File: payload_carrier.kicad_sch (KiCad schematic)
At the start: 44 parts, among them J1 Conn_01x02, J2 USB_C_Receptacle_USB2.0_16P, J3 Conn_01x08, J4 Conn_01x08, J5 Conn_01x05, J6 Micro_SD_Card, SW1 SW_MEC_5G, U1 TPS73733DCQR, U2 TPS562242DRLR, U3 STM32G0B1CBTx, Y1 Crystal

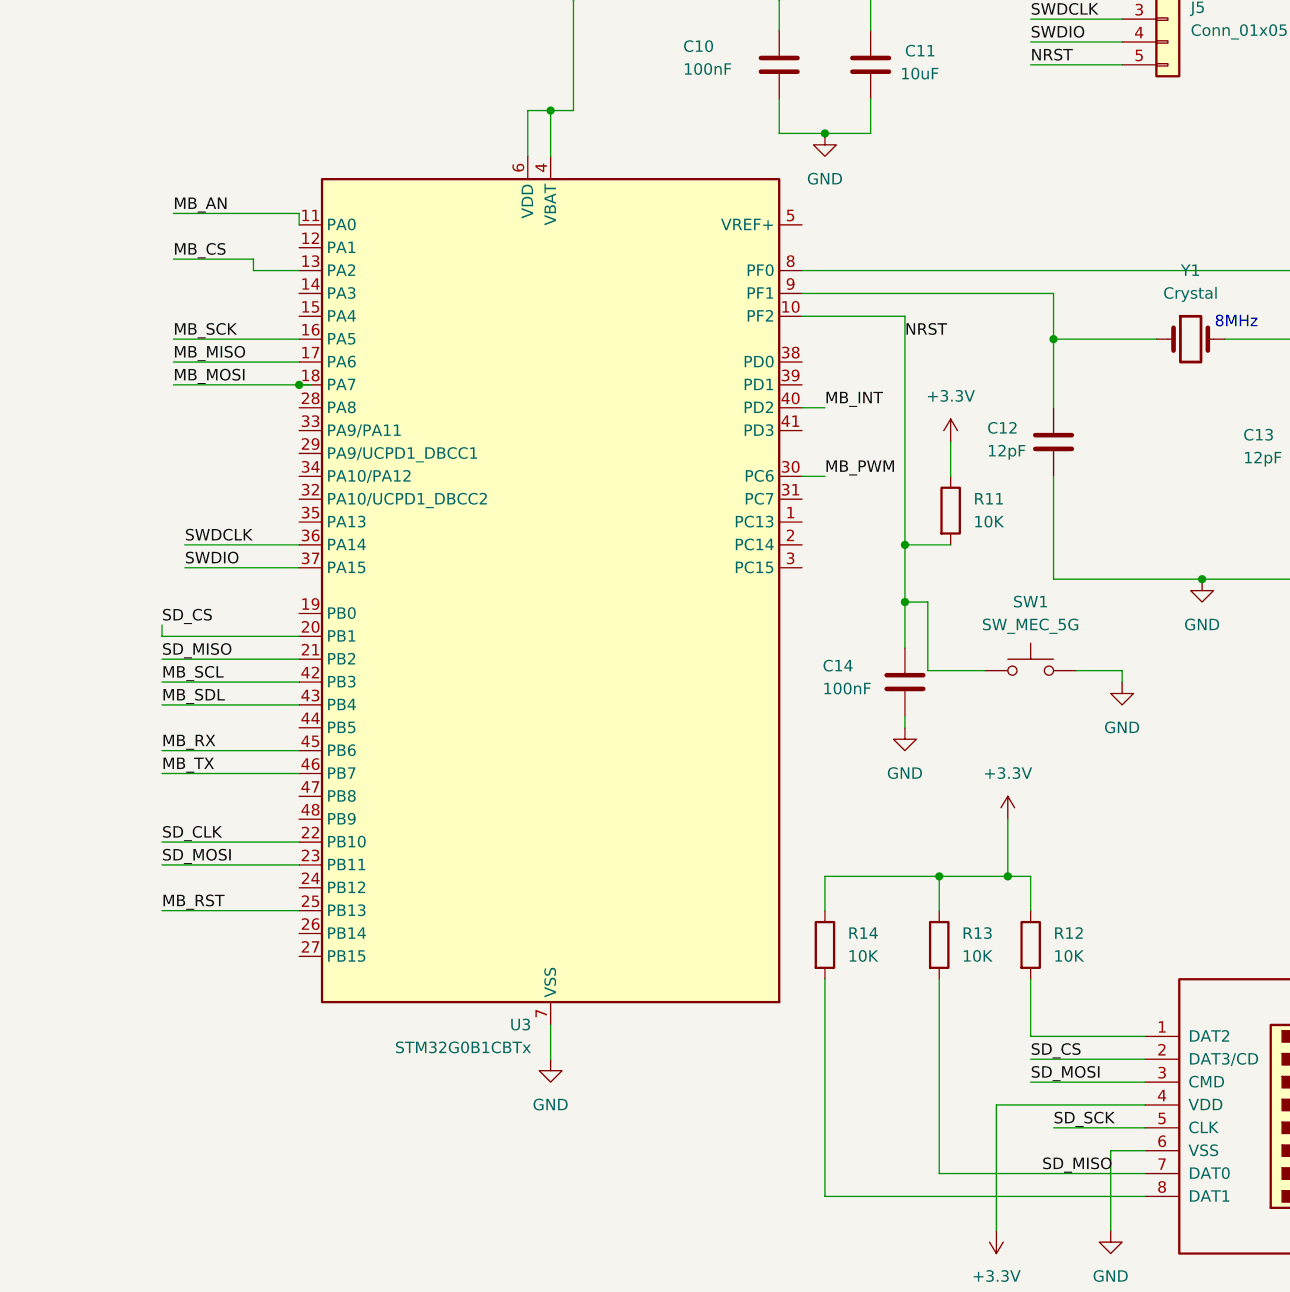
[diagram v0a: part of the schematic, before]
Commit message: Fix net bugs and assign footprints for layout session
- SD_SCK label -> SD_CLK: SD card CLK now reaches PB10
- MB_SDL label -> MB_SDA: PB4 now reaches mikroBUS SDA
- SWDIO moved from PA15 to PA13
- U1 footprint uses project lib nickname "My footprints"
- VREF+ tied to +3.3V with new C15 100nF decoupling
- Footprints on all parts except R11, C10, U2 (left for the
  footprint demo; stock 0603 R/C and SOT-563)
- Y1 on 2-pad 5032 crystal, SW1 on SW_MEC_5GSH9 (pads match symbol),
  D1/D2 on SMA (value should read B340A)

Co-Authored-By: Claude Opus 5.5 <noreply@anthropic.com>
Claude-Session: https://claude.ai/code/session_01BZgeQ4ki9vnPRRu7w6dazn
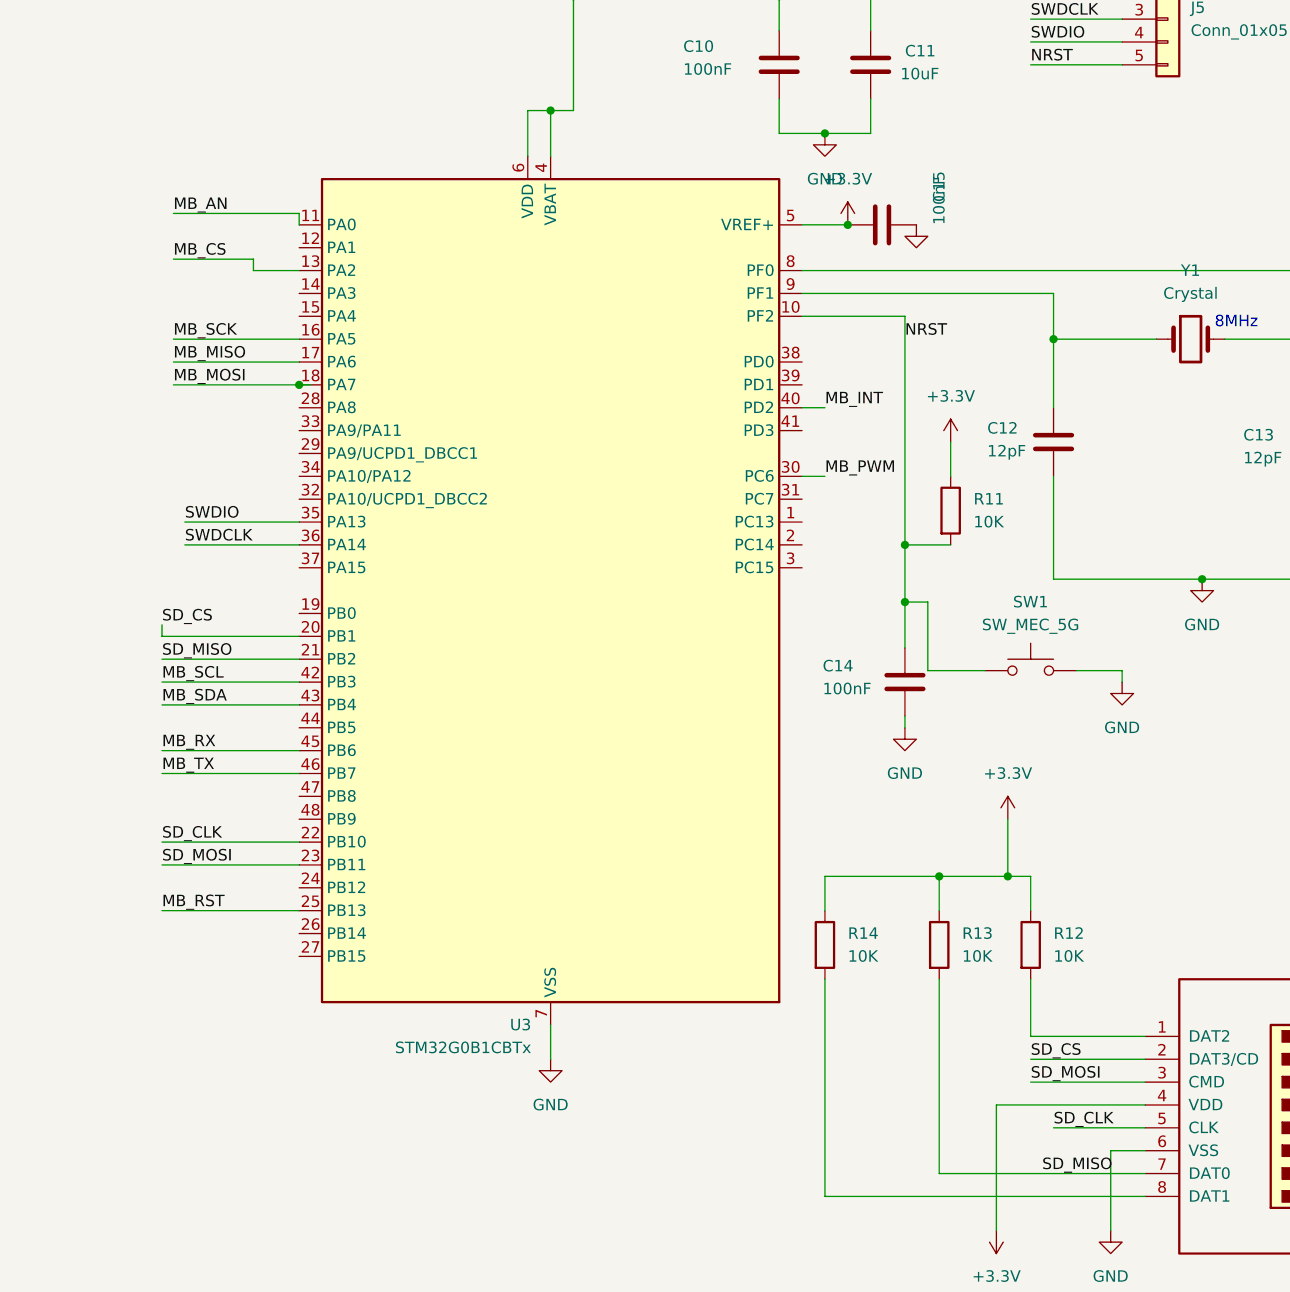
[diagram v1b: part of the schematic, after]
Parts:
- added C15: 100nF, Capacitor_SMD:C_0603_1608Metric, symbol KiCad:C
- C1, C12, C13, C14, C2, C3, C6, C7, C9: footprint (none) -> Capacitor_SMD:C_0603_1608Metric
- C11, C4, C5, C8: footprint (none) -> Capacitor_SMD:C_0805_2012Metric
- D1, D2: footprint (none) -> Diode_SMD:D_SMA
- D3, D4: footprint (none) -> LED_SMD:LED_0603_1608Metric
- J1: footprint (none) -> Connector_JST:JST_PH_B2B-PH-K_1x02_P2.00mm_Vertical
- J2: footprint (none) -> Connector_USB:USB_C_Receptacle_HRO_TYPE-C-31-M-12
- J3, J4: footprint (none) -> Connector_PinSocket_2.54mm:PinSocket_1x08_P2.54mm_Vertical
- J5: footprint (none) -> Connector_PinHeader_2.54mm:PinHeader_1x05_P2.54mm_Vertical
- J6: footprint (none) -> Connector_Card:microSD_HC_Wuerth_693072010801
- L1: footprint (none) -> Inductor_SMD:L_Bourns-SRN4018
- R1, R10, R12, R13, R14, R2, R3, R4, R5, R6, R7, R8, R9: footprint (none) -> Resistor_SMD:R_0603_1608Metric
- SW1: footprint (none) -> Button_Switch_SMD:SW_MEC_5GSH9
- U1: footprint TPS73733DCQR:IC_TPS73733DCQR -> My footprints:IC_TPS73733DCQR
- U2: footprint Package_TO_SOT_SMD:SOT-563 -> (none)
- Y1: footprint (none) -> Crystal:Crystal_SMD_5032-2Pin_5.0x3.2mm
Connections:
- net MB_SDL is gone; now on net MB_SDA: U3.43 (PB4)
- net SD_SCK is gone; now on net SD_CLK: J6.5 (CLK)
- net +3.3V: now also U3.5 (VREF+), C15.1
- net GND: now also C15.2
- net SWDIO: now also U3.35 (PA13); no longer U3.37 (PA15)

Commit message: Wire USB data to STM32, add buck feedforward cap, pick L1
- J2 D+ (A6/B6) -> PA12 (USB_DP), D- (A7/B7) -> PA11 (USB_DM);
  removed the four no-connect flags
- C16 33pF across R3 (TI TPS562242 Table 8-2, 5 V row)
- L1: Wurth WE-MAPI 4020 74438356033 (3.3uH, Isat 3.55A @10%),
  footprint Inductor_SMD:L_Wuerth_MAPI-4020

Co-Authored-By: Claude Opus 5.5 <noreply@anthropic.com>
Claude-Session: https://claude.ai/code/session_01BZgeQ4ki9vnPRRu7w6dazn
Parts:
- added C16: 33pF, Capacitor_SMD:C_0603_1608Metric, symbol KiCad:C
- L1: footprint Inductor_SMD:L_Bourns-SRN4018 -> Inductor_SMD:L_Wuerth_MAPI-4020
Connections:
- net at C8.1, C9.1, D1.2 (A)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: now also C16.1
- net USB_DM: now reaches U3.33 (PA9/PA11)
- net USB_DM: now also J2.A7 (D-), J2.B7 (D-)
- net USB_DP: now reaches U3.34 (PA10/PA12)
- net USB_DP: now also J2.A6 (D+), J2.B6 (D+)
- net at R3.2, R4.1, U2.6 (VFB): now also C16.2
- no-connect marks 6 -> 2
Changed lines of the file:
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@@
 	)
 	(no_connect
-		(at 199.39 76.2)
-	)
-	(no_connect
 		(at 209.55 76.2)
 	)
 	(no_connect
-		(at 194.31 76.2)
-	)
-	(no_connect
-		(at 196.85 76.2)
-	)
-	(no_connect
-		(at 191.77 76.2)
-	)
-	(no_connect
 		(at 207.01 76.2)
 	)
@@
 			)
 		)
-		(property "Footprint" "Inductor_SMD:L_Bourns-SRN4018"
+		(property "Footprint" "Inductor_SMD:L_Wuerth_MAPI-4020"
 			(at 166.37 33.02 0)
 			(hide yes)
@@
 			)
 		)
-		(property "Datasheet" ""
+		(property "Datasheet" "https://www.we-online.com/components/products/datasheet/74438356033.pdf"
 			(at 166.37 33.02 0)
 			(hide yes)
@@
 			)
 		)
-		(property "Description" "Inductor"
+		(property "Description" "Inductor, Wurth WE-MAPI 4020 74438356033, 3.3uH, Isat 3.55A"
 			(at 166.37 33.02 0)
 			(hide yes)
@@
 		)
 	)
+	(wire
+		(pts
+			(xy 191.77 76.2) (xy 191.77 73.66)
+		)
+		(stroke
+			(width 0)
+			(type default)
+		)
+	)
+	(wire
+		(pts
+			(xy 194.31 76.2) (xy 194.31 73.66)
+		)
+		(stroke
+			(width 0)
+			(type default)
+		)
+	)
+	(wire
+		(pts
+			(xy 191.77 73.66) (xy 194.31 73.66)
+		)
+		(stroke
+			(width 0)
+			(type default)
+		)
+	)
+	(label "USB_DM"
+		(at 191.77 73.66 0)
+		(effects
+			(font
+				(size 1.27 1.27)
+			)
+			(justify left bottom)
+		)
+	)
+	(wire
+		(pts
+			(xy 196.85 76.2) (xy 196.85 74.93)
+		)
+		(stroke
+			(width 0)
+			(type default)
+		)
+	)
+	(wire
+		(pts
+			(xy 199.39 76.2) (xy 199.39 74.93)
+		)
+		(stroke
+			(width 0)
+			(type default)
+		)
+	)
+	(wire
+		(pts
+			(xy 196.85 74.93) (xy 199.39 74.93)
+		)
+		(stroke
+			(width 0)
+			(type default)
+		)
+	)
+	(label "USB_DP"
+		(at 199.39 74.93 0)
+		(effects
+			(font
+				(size 1.27 1.27)
+			)
+			(justify left bottom)
+		)
+	)
+	(wire
+		(pts
+			(xy 71.12 182.88) (xy 83.82 182.88)
+		)
+		(stroke
+			(width 0)
+			(type default)
+		)
+	)
+	(label "USB_DM"
+		(at 71.12 182.88 0)
+		(effects
+			(font
+				(size 1.27 1.27)
+			)
+			(justify left bottom)
+		)
+	)
+	(wire
+		(pts
+			(xy 71.12 187.96) (xy 83.82 187.96)
+		)
+		(stroke
+			(width 0)
+			(type default)
+		)
+	)
+	(label "USB_DP"
+		(at 71.12 187.96 0)
+		(effects
+			(font
+				(size 1.27 1.27)
+			)
+			(justify left bottom)
+		)
+	)
+	(symbol
+		(lib_id "KiCad:C")
+		(at 171.45 40.64 0)
+		(unit 1)
+		(body_style 1)
+		(exclude_from_sim no)
+		(in_bom yes)
+		(on_board yes)
+		(in_pos_files yes)
+		(dnp no)
+		(property "Reference" "C16"
+			(at 162.56 39.37 0)
+			(show_name no)
+			(do_not_autoplace no)
+			(effects
+				(font
+					(size 1.27 1.27)
+				)
+				(justify left)
+			)
+		)
+		(property "Value" "33pF"
+			(at 162.56 41.91 0)
+			(show_name no)
+			(do_not_autoplace no)
+			(effects
+				(font
+					(size 1.27 1.27)
+				)
+				(justify left)
+			)
+		)
+		(property "Footprint" "Capacitor_SMD:C_0603_1608Metric"
+			(at 172.4152 44.45 0)
+			(hide yes)
+			(show_name no)
+			(do_not_autoplace no)
+			(effects
+				(font
+					(size 1.27 1.27)
+				)
+			)
+		)
+		(property "Datasheet" ""
+			(at 171.45 40.64 0)
+			(hide yes)
+			(show_name no)
+			(do_not_autoplace no)
+			(effects
+				(font
+					(size 1.27 1.27)
+				)
+			)
+		)
+		(property "Description" "Unpolarized capacitor"
+			(at 171.45 40.64 0)
+			(hide yes)
+			(show_name no)
+			(do_not_autoplace no)
+			(effects
+				(font
+					(size 1.27 1.27)
+				)
+			)
+		)
+		(pin "1"
+		)
+		(pin "2"
+		)
+		(instances
+			(project "payload_carrier"
+				(path "/a2cb1e14-d4cf-4893-8103-046de657b74e"
+					(reference "C16")
+					(unit 1)
+				)
+			)
+		)
+	)
+	(wire
+		(pts
+			(xy 171.45 36.83) (xy 176.53 36.83)
+		)
+		(stroke
+			(width 0)
+			(type default)
+		)
+	)
+	(junction
+		(at 176.53 36.83)
+		(diameter 0)
+		(color 0 0 0 0)
+	)
+	(wire
+		(pts
+			(xy 171.45 44.45) (xy 176.53 44.45)
+		)
+		(stroke
+			(width 0)
+			(type default)
+		)
+	)
+	(junction
+		(at 176.53 44.45)
+		(diameter 0)
+		(color 0 0 0 0)
+	)
 	(sheet_instances

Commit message: D1/D2 value B340 -> B340A to match SMA footprint
Co-Authored-By: Claude Opus 5.5 <noreply@anthropic.com>
Claude-Session: https://claude.ai/code/session_01BZgeQ4ki9vnPRRu7w6dazn
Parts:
- D1, D2: value B340 -> B340A
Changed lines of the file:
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@@
 			)
 		)
-		(property "Value" "B340"
+		(property "Value" "B340A"
 			(at 171.45 66.04 0)
 			(show_name no)
@@
 			)
 		)
-		(property "Value" "B340"
+		(property "Value" "B340A"
 			(at 207.01 29.21 0)
 			(show_name no)
